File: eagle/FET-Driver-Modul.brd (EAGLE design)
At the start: 75.2 x 60 mm, 19 parts, among them X1 MKDSN1,5/3-5,08

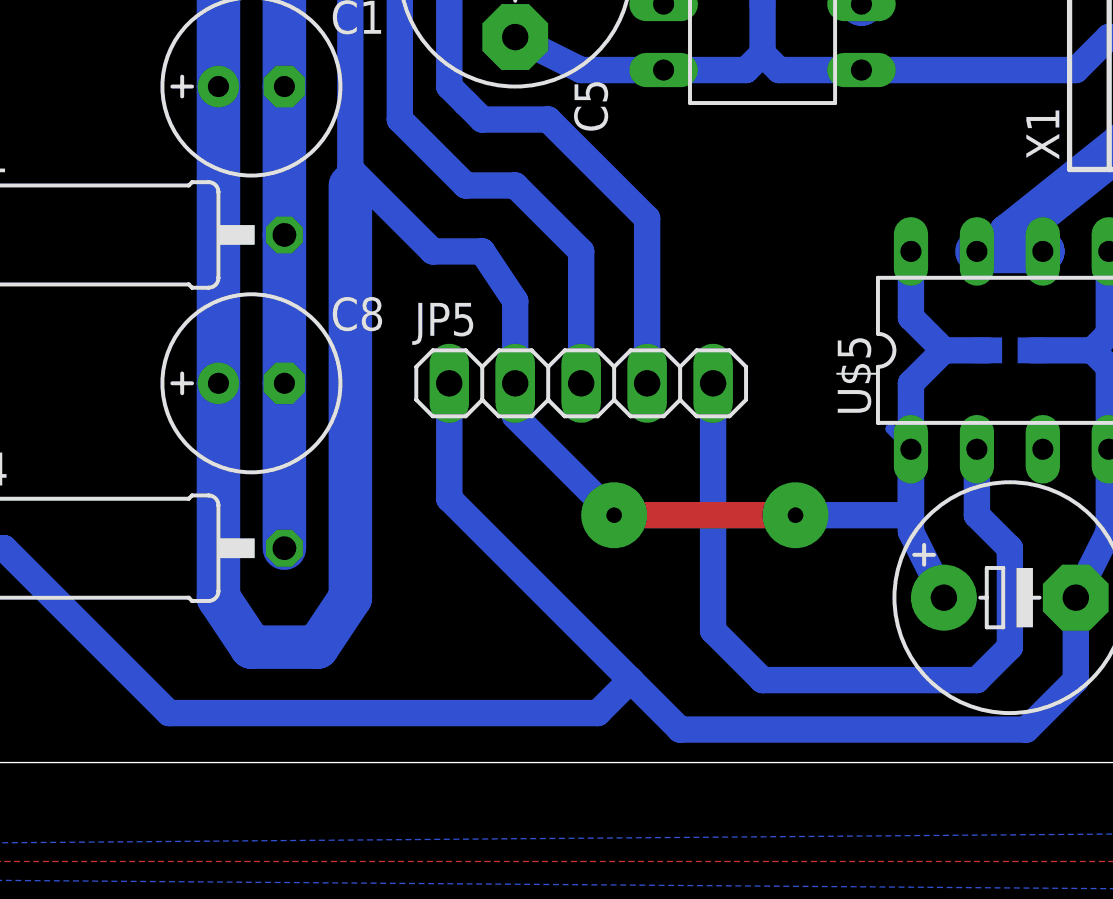
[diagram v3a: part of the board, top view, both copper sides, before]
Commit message: additional diode at Mosfet driver
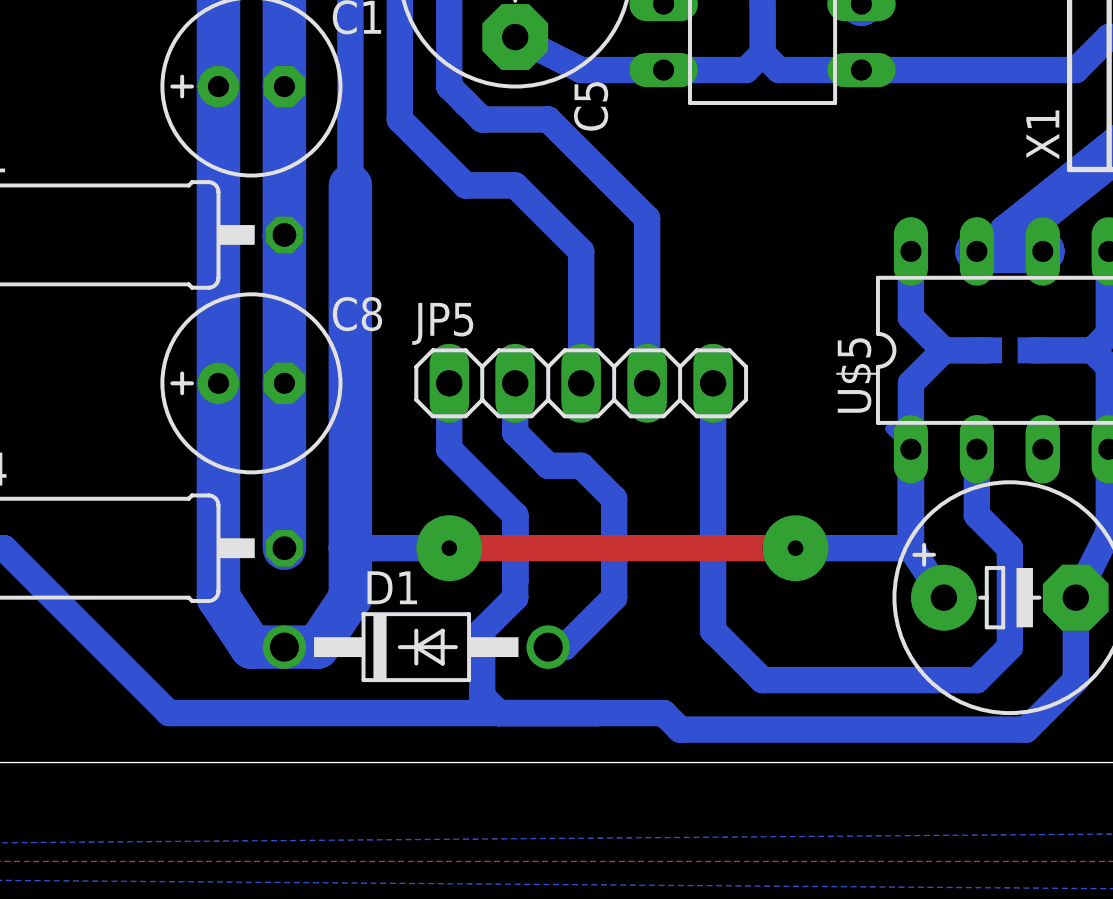
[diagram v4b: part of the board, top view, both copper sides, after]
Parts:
- added D1: 1N4004, diode:DO41-10
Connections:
- new net N$6: D1.A, JP5.2
- net N$2: now also D1.C; no longer JP5.2
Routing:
- net N$6: track 0.00 -> 13.9 mm
- net N$2: track 245.4 -> 238.4 mm
- net GND: track 263.7 -> 269.2 mm
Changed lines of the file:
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@@
 <element name="R3" library="resistor" package="0411/15" value="150" x="11.43" y="43.18"/>
 <element name="R4" library="resistor" package="0411/15" value="150" x="11.43" y="8.255"/>
+<element name="D1" library="diode" package="DO41-10" value="1N4004" x="24.13" y="4.445"/>
 </elements>
 <signals>
@@
 <wire x1="43.18" y1="52.07" x2="44.45" y2="54.61" width="1.016" layer="16"/>
 <contactref element="JP5" pad="1"/>
-<wire x1="25.4" y1="14.605" x2="25.4" y2="10.16" width="1.016" layer="16"/>
-<wire x1="25.4" y1="10.16" x2="32.385" y2="3.175" width="1.016" layer="16"/>
-<wire x1="32.385" y1="3.175" x2="34.29" y2="1.27" width="1.016" layer="16"/>
 <wire x1="34.29" y1="1.27" x2="47.625" y2="1.27" width="1.016" layer="16"/>
 <wire x1="47.625" y1="1.27" x2="49.53" y2="3.175" width="1.016" layer="16"/>
@@
 <wire x1="3.81" y1="8.255" x2="8.255" y2="8.255" width="1.016" layer="16"/>
 <wire x1="8.255" y1="8.255" x2="14.605" y2="1.905" width="1.016" layer="16"/>
-<wire x1="14.605" y1="1.905" x2="31.115" y2="1.905" width="1.016" layer="16"/>
-<wire x1="31.115" y1="1.905" x2="32.385" y2="3.175" width="1.016" layer="16"/>
+<wire x1="14.605" y1="1.905" x2="27.305" y2="1.905" width="1.016" layer="16"/>
+<wire x1="27.305" y1="1.905" x2="31.115" y2="1.905" width="1.016" layer="16"/>
 <contactref element="C5" pad="-"/>
 <contactref element="C6" pad="2"/>
@@
 <wire x1="57.15" y1="21.59" x2="55.245" y2="19.685" width="1.016" layer="16"/>
 <wire x1="55.245" y1="19.685" x2="50.8" y2="19.685" width="1.016" layer="16"/>
+<wire x1="25.4" y1="14.605" x2="25.4" y2="12.065" width="1.016" layer="16"/>
+<wire x1="25.4" y1="12.065" x2="27.94" y2="9.525" width="1.016" layer="16"/>
+<wire x1="27.94" y1="9.525" x2="27.94" y2="6.985" width="1.016" layer="16"/>
+<wire x1="34.29" y1="1.27" x2="33.655" y2="1.905" width="1.016" layer="16"/>
+<wire x1="33.655" y1="1.905" x2="31.115" y2="1.905" width="1.016" layer="16"/>
+<wire x1="31.115" y1="1.905" x2="27.305" y2="1.905" width="1.016" layer="16"/>
+<wire x1="27.305" y1="1.905" x2="26.67" y2="2.54" width="1.016" layer="16"/>
+<wire x1="26.67" y1="2.54" x2="26.67" y2="5.08" width="1.016" layer="16"/>
+<wire x1="26.67" y1="5.08" x2="27.94" y2="6.35" width="1.016" layer="16"/>
+<wire x1="27.94" y1="6.35" x2="27.94" y2="6.985" width="1.016" layer="16"/>
+<wire x1="27.94" y1="6.985" x2="27.94" y2="9.525" width="1.016" layer="16"/>
 </signal>
 <signal name="N$16">
@@
 <wire x1="44.45" y1="15.875" x2="43.18" y2="17.145" width="1.016" layer="16"/>
 <wire x1="43.18" y1="17.145" x2="43.18" y2="19.685" width="1.016" layer="16"/>
-<wire x1="43.18" y1="12.065" x2="43.18" y2="9.525" width="1.016" layer="16"/>
-<wire x1="43.18" y1="9.525" x2="43.18" y2="8.89" width="1.016" layer="16"/>
-<wire x1="43.18" y1="8.89" x2="44.45" y2="6.35" width="1.016" layer="16"/>
+<wire x1="43.18" y1="12.065" x2="43.18" y2="8.255" width="1.016" layer="16"/>
+<wire x1="43.18" y1="8.255" x2="44.45" y2="6.35" width="1.016" layer="16"/>
 <wire x1="42.393" y1="12.852" x2="43.18" y2="12.065" width="0.4064" layer="16"/>
 <contactref element="U$3" pad="8"/>
@@
 <wire x1="34.29" y1="34.29" x2="36.83" y2="34.29" width="1.016" layer="16"/>
 <wire x1="36.83" y1="34.29" x2="37.465" y2="33.655" width="1.016" layer="16"/>
-<contactref element="JP5" pad="2"/>
 <contactref element="C1" pad="+"/>
 <contactref element="C2" pad="+"/>
@@
 <via x="25.4" y="41.275" extent="1-16" drill="0.6" diameter="2.54" shape="octagon"/>
 <wire x1="25.4" y1="41.275" x2="22.86" y2="41.275" width="1.016" layer="16"/>
-<wire x1="27.94" y1="14.605" x2="27.94" y2="13.335" width="1.016" layer="16"/>
-<wire x1="27.94" y1="13.335" x2="31.75" y2="9.525" width="1.016" layer="16"/>
-<via x="31.75" y="9.525" extent="1-16" drill="0.6" diameter="2.54" shape="octagon"/>
-<wire x1="31.75" y1="9.525" x2="38.735" y2="9.525" width="1.016" layer="1"/>
-<via x="38.735" y="9.525" extent="1-16" drill="0.6" diameter="2.54" shape="octagon"/>
-<wire x1="38.735" y1="9.525" x2="43.18" y2="9.525" width="1.016" layer="16"/>
-<wire x1="43.18" y1="9.525" x2="43.18" y2="12.065" width="1.016" layer="16"/>
-<wire x1="27.94" y1="14.605" x2="27.94" y2="17.78" width="1.016" layer="16"/>
-<wire x1="27.94" y1="17.78" x2="26.67" y2="19.685" width="1.016" layer="16"/>
-<wire x1="26.67" y1="19.685" x2="24.765" y2="19.685" width="1.016" layer="16"/>
-<wire x1="24.765" y1="19.685" x2="21.59" y2="22.86" width="1.016" layer="16"/>
+<via x="25.4" y="8.255" extent="1-16" drill="0.6" diameter="2.54" shape="octagon"/>
+<wire x1="25.4" y1="8.255" x2="38.735" y2="8.255" width="1.016" layer="1"/>
+<via x="38.735" y="8.255" extent="1-16" drill="0.6" diameter="2.54" shape="octagon"/>
+<wire x1="38.735" y1="8.255" x2="43.18" y2="8.255" width="1.016" layer="16"/>
+<wire x1="43.18" y1="8.255" x2="43.18" y2="12.065" width="1.016" layer="16"/>
 <wire x1="21.59" y1="22.86" x2="21.59" y2="40.005" width="1.016" layer="16"/>
 <wire x1="21.59" y1="40.005" x2="22.86" y2="41.275" width="1.016" layer="16"/>
@@
 <wire x1="17.78" y1="4.445" x2="20.32" y2="4.445" width="1.6764" layer="16"/>
 <wire x1="20.32" y1="4.445" x2="21.59" y2="6.35" width="1.6764" layer="16"/>
-<wire x1="21.59" y1="6.35" x2="21.59" y2="22.225" width="1.6764" layer="16"/>
+<wire x1="21.59" y1="6.35" x2="21.59" y2="8.255" width="1.6764" layer="16"/>
+<contactref element="D1" pad="C"/>
+<wire x1="21.59" y1="8.255" x2="21.59" y2="22.225" width="1.6764" layer="16"/>
+<wire x1="25.4" y1="8.255" x2="21.59" y2="8.255" width="1.016" layer="16"/>
+<wire x1="19.05" y1="4.445" x2="20.32" y2="4.445" width="0" layer="19" extent="16-16"/>
 </signal>
 <signal name="N$1">
@@
 <wire x1="46.99" y1="52.705" x2="48.26" y2="51.435" width="1.016" layer="16"/>
 </signal>
+<signal name="N$6">
+<contactref element="JP5" pad="2"/>
+<contactref element="D1" pad="A"/>
+<wire x1="27.94" y1="14.605" x2="27.94" y2="12.7" width="1.016" layer="16"/>
+<wire x1="27.94" y1="12.7" x2="29.21" y2="11.43" width="1.016" layer="16"/>
+<wire x1="29.21" y1="11.43" x2="30.48" y2="11.43" width="1.016" layer="16"/>
+<wire x1="30.48" y1="11.43" x2="31.75" y2="10.16" width="1.016" layer="16"/>
+<wire x1="31.75" y1="10.16" x2="31.75" y2="6.35" width="1.016" layer="16"/>
+<wire x1="31.75" y1="6.35" x2="29.845" y2="4.445" width="1.016" layer="16"/>
+<wire x1="29.845" y1="4.445" x2="29.21" y2="4.445" width="1.016" layer="16"/>
+</signal>
 </signals>
